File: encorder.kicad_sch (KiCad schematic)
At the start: 3 parts, among them J11 Conn_01x06_Pin, U1 MA730

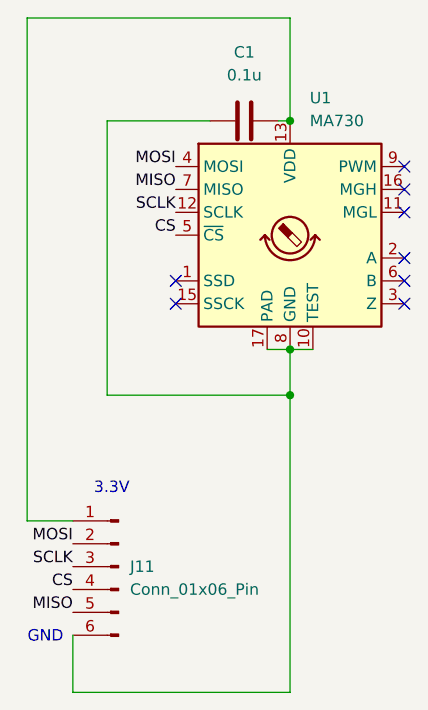
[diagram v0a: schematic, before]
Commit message: 壁センサ修正
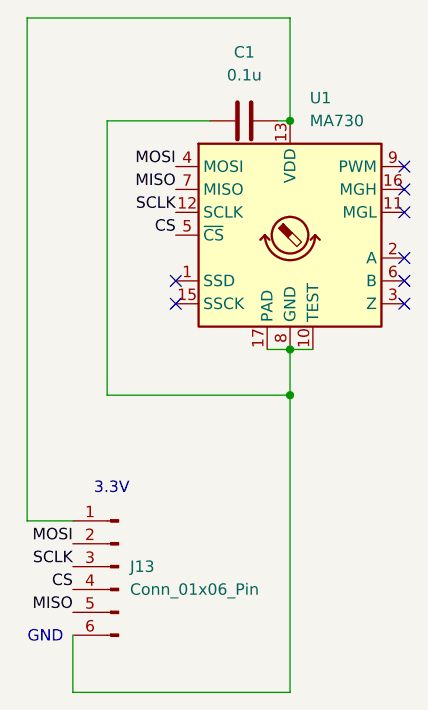
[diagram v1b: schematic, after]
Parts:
- renumbered J11 to J13
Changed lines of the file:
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@@
 		(dnp no)
 		(fields_autoplaced yes)
-		(property "Reference" "J11"
+		(property "Reference" "J13"
 			(at 120.65 127 0)
 			(effects
